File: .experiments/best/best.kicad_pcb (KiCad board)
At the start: 2 copper layers, 140 x 90 mm, 39 parts, among them J1 USB_C, J2 Output, J3 Debug, Q1 FS8205A, U1 USBLC6-2SC6, U2 BQ24072, U3 HY2113-KB5B, U4 MT3608, U5 AP2112K-3.3, U6 LN61CN3302MR-G

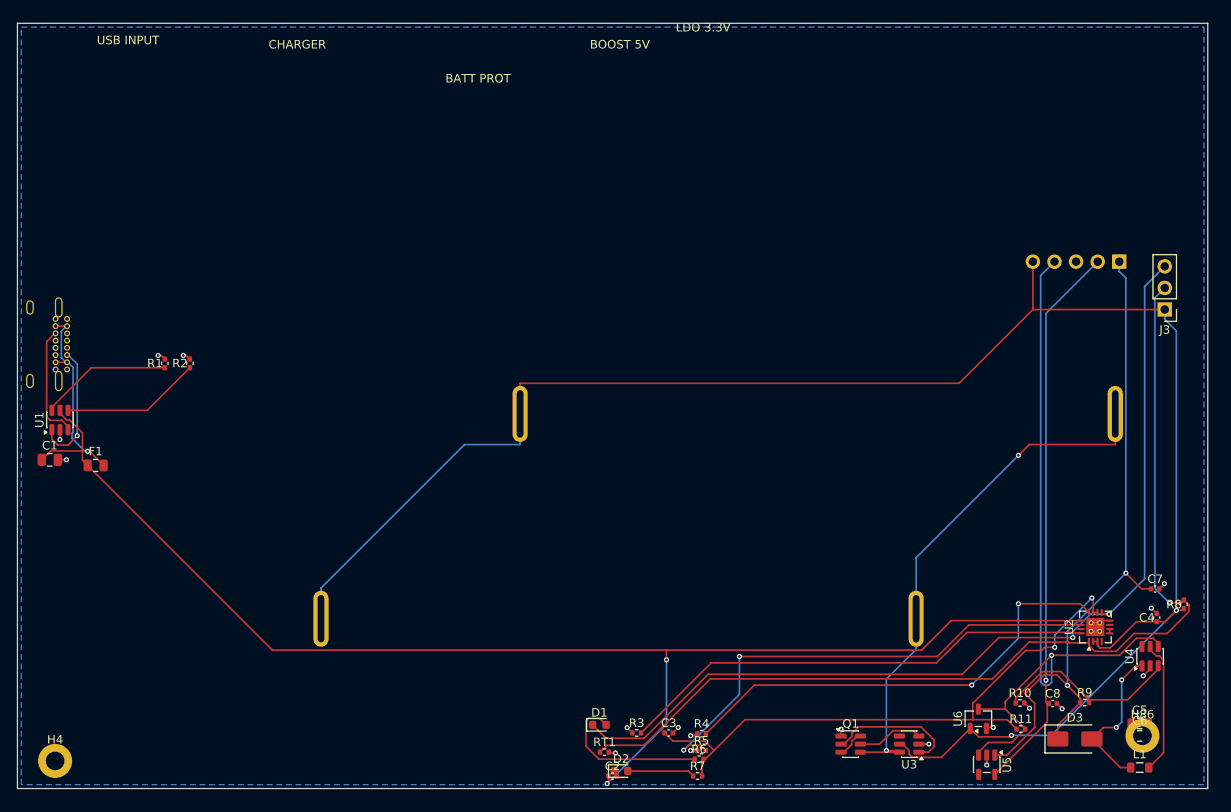
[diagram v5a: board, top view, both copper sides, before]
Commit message: trimed version seems to have broken grouping and group labeling
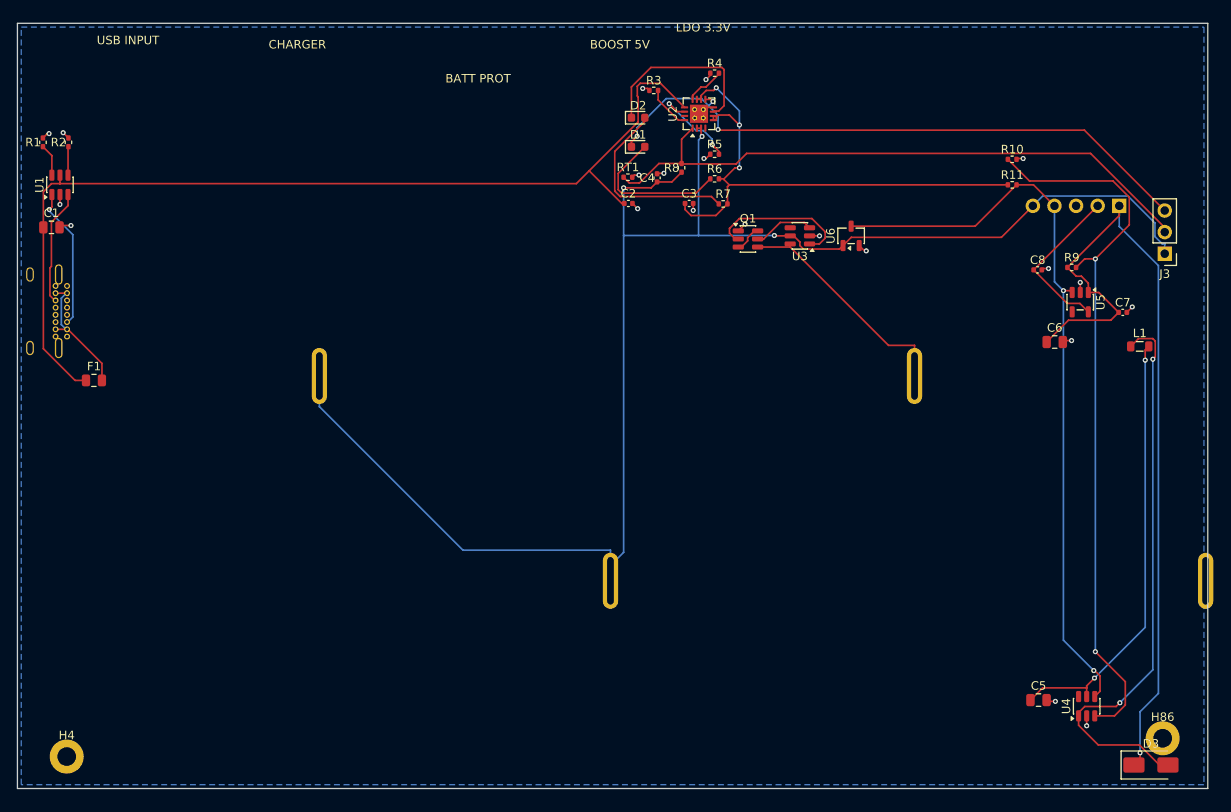
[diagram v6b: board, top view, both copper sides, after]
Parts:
- moved C4 78.3 mm to (75.2, 18.2)
- moved R8 78.3 mm to (78.1, 17.0)
- moved R4 77.7 mm to (82.0, 5.87)
- moved D2 76.9 mm to (73.0, 11.1)
- moved U2 76.3 mm to (80.2, 10.6)
- moved R3 75.6 mm to (74.8, 7.90)
- moved R5 70.1 mm to (82.0, 15.4)
- moved R6 68.3 mm to (82.0, 18.3)
- moved D1 68.1 mm to (73.0, 14.5)
- moved RT1 67.7 mm to (71.8, 18.1)
- moved C2 67.4 mm to (71.9, 21.2)
- moved R7 67.4 mm to (83.0, 21.2)
- moved R11 64.0 mm to (117.0, 19.0)
- moved R10 63.9 mm to (117.0, 16.0)
- moved C3 62.3 mm to (79.0, 21.2)
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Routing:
- net Net-(U4-FB): track 22.2 -> 85.8 mm, vias 0 -> 2
- net Net-(U2-ISET): track 56.7 -> 5.21 mm
- net Net-(U2-ILIM): track 54.2 -> 4.70 mm, vias 2 -> 0
- net Net-(D3-A): track 18.3 -> 66.9 mm
- net Net-(U2-TMR): track 58.5 -> 11.1 mm
- net /3V3: track 65.6 -> 19.1 mm, vias 1 -> 0
- net /NTC_SENSE: track 119.1 -> 74.2 mm, vias 1 -> 0
- net /VBUS: track 160.1 -> 116.2 mm, vias 2 -> 0
- net /CHG_N: track 112.4 -> 74.2 mm, vias 2 -> 3
- net /CELL_NEG: track 62.9 -> 27.2 mm, vias 2 -> 0
- net /VSYS_BOOST: track 15.8 -> 51.4 mm, vias 0 -> 2
- net /VBAT: track 216.8 -> 186.0 mm, vias 2 -> 3
- net Net-(D2-K): track 0.00 -> 21.4 mm
- net /5V: track 81.6 -> 97.4 mm, vias 2 -> 1
- net Net-(D2-A): track 7.95 -> 23.0 mm
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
